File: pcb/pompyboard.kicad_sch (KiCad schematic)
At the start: 14 parts, among them J1 USB_C_Receptacle_USB2.0_16P, J2 Conn_01x04_Pin, SW1 EVQQ2B03W, U229 STM32F429IGT6, U231 AMS1117CD-3.3

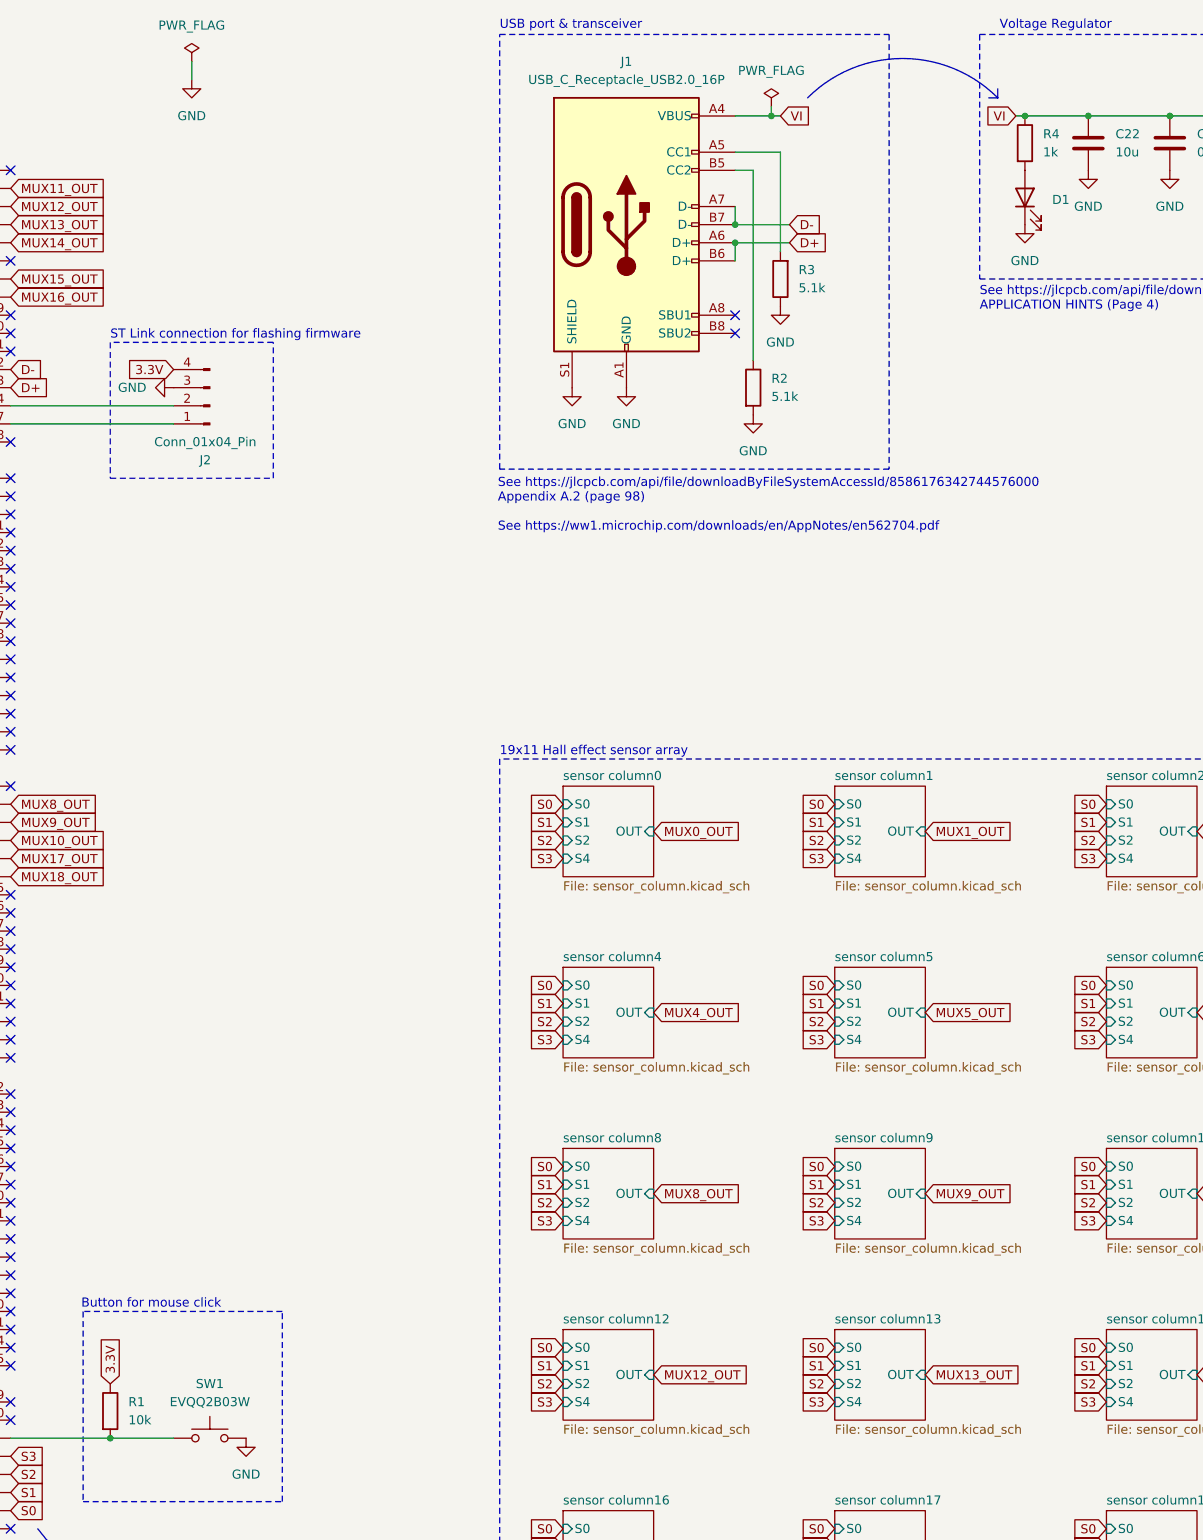
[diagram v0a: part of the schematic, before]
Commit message: pcb: add resistors to reduce multiplexer channel crosstalk
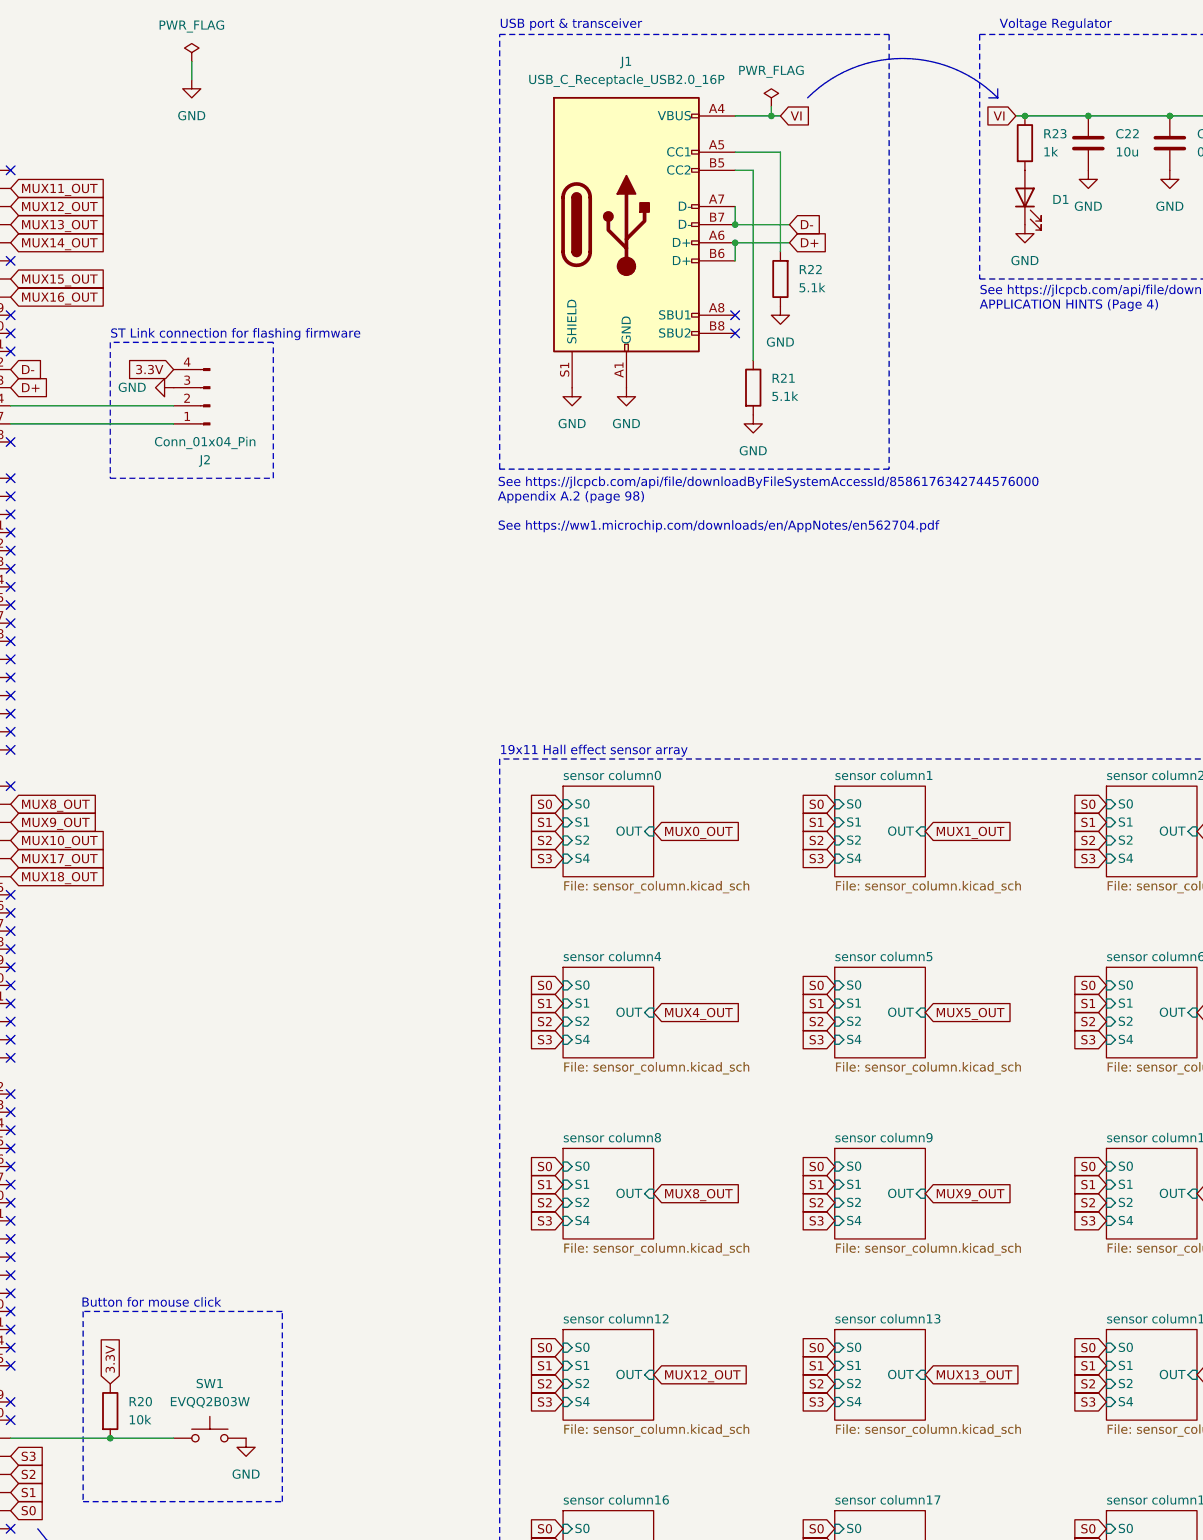
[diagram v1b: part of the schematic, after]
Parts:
- renumbered R1 to R20, R2 to R21, R3 to R22, R4 to R23
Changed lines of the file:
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@@
 		(dnp no)
 		(fields_autoplaced yes)
-		(property "Reference" "R3"
+		(property "Reference" "R22"
 			(at 219.71 58.4199 0)
 			(effects
@@
 			(project "pompyboard"
 				(path "/e5830f2e-b6bc-440e-bdf9-7651ab21e3a0"
-					(reference "R3")
+					(reference "R22")
 					(unit 1)
 				)
@@
 		(dnp no)
 		(fields_autoplaced yes)
-		(property "Reference" "R1"
+		(property "Reference" "R20"
 			(at 125.73 217.1699 0)
 			(effects
@@
 			(project ""
 				(path "/e5830f2e-b6bc-440e-bdf9-7651ab21e3a0"
-					(reference "R1")
+					(reference "R20")
 					(unit 1)
 				)
@@
 		(dnp no)
 		(fields_autoplaced yes)
-		(property "Reference" "R4"
+		(property "Reference" "R23"
 			(at 254 39.3699 0)
 			(effects
@@
 			(project "pompyboard"
 				(path "/e5830f2e-b6bc-440e-bdf9-7651ab21e3a0"
-					(reference "R4")
+					(reference "R23")
 					(unit 1)
 				)
@@
 		(dnp no)
 		(fields_autoplaced yes)
-		(property "Reference" "R2"
+		(property "Reference" "R21"
 			(at 215.9 73.6599 0)
 			(effects
@@
 			(project ""
 				(path "/e5830f2e-b6bc-440e-bdf9-7651ab21e3a0"
-					(reference "R2")
-					(unit 1)
-				)
+					(reference "R21")
+					(unit 1)
+				)

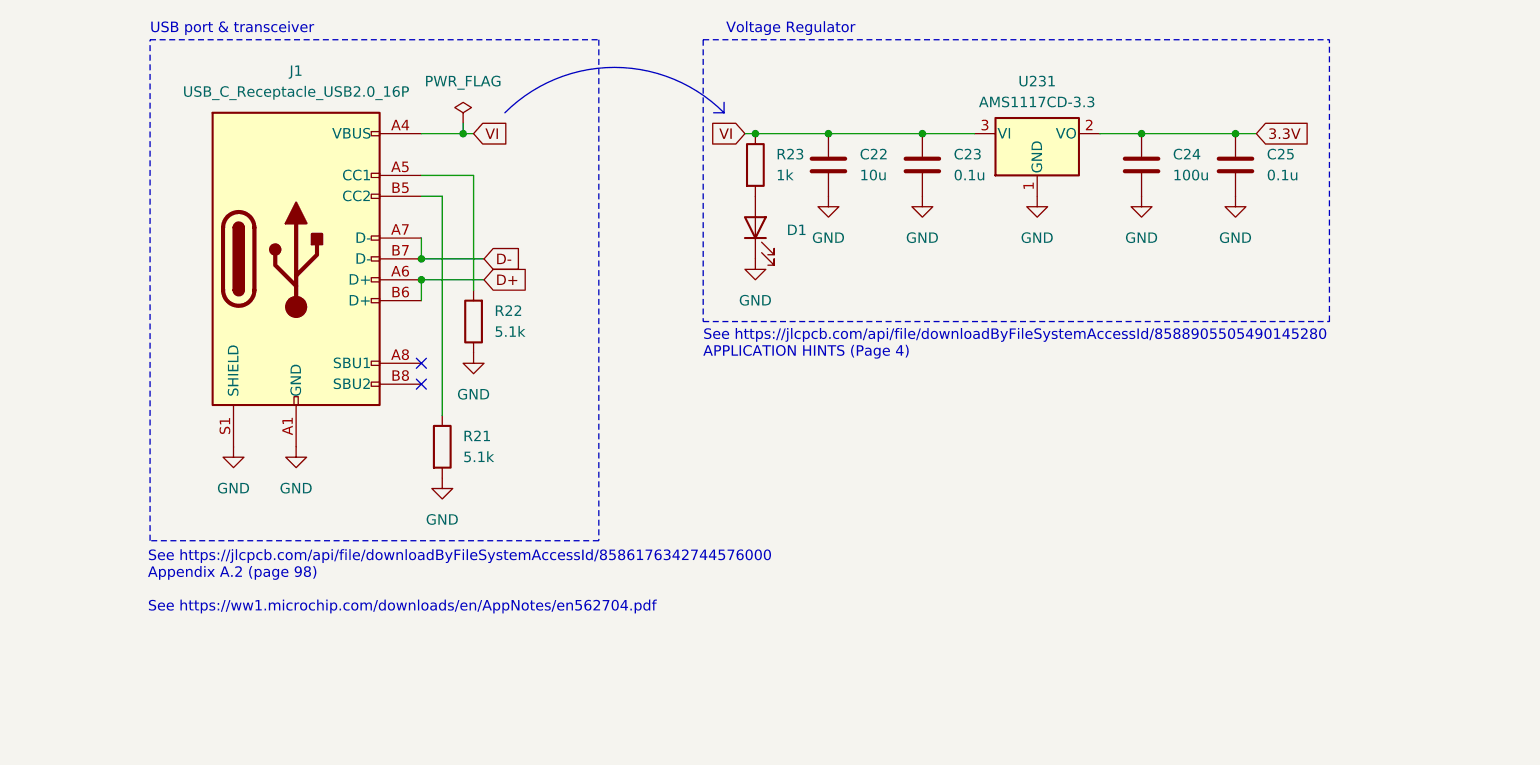
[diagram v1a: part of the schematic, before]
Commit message: pcb: replace LDO with buck converter to improve power efficiency
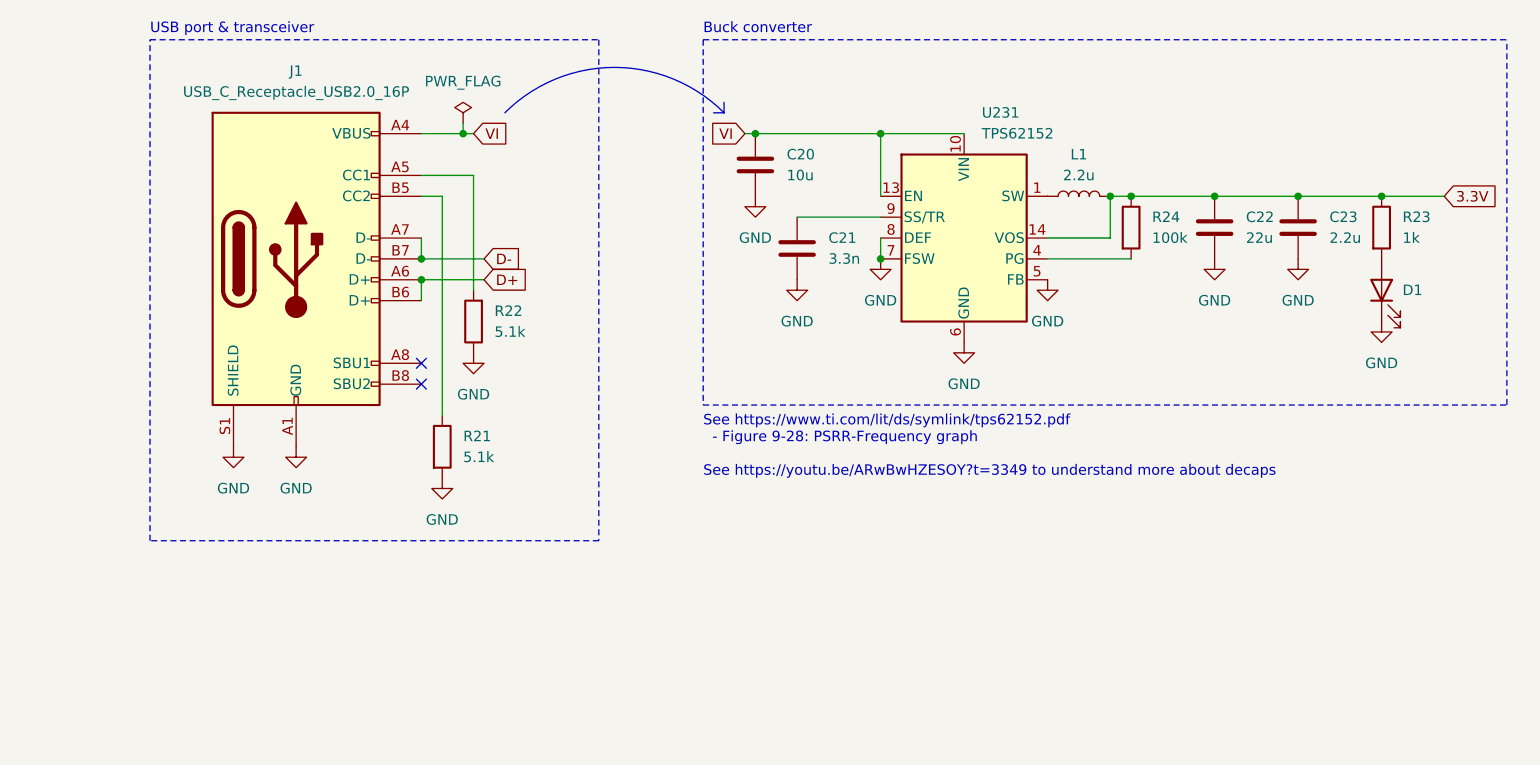
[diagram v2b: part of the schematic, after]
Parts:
- removed C25: 0.1u, Capacitor_SMD:C_0402_1005Metric, symbol Device:C
- removed U231: AMS1117CD-3.3, Package_TO_SOT_SMD:TO-252-3_TabPin2, symbol Regulator_Linear:AMS1117CD-3.3
- added C21: 3.3n, Capacitor_SMD:C_0402_1005Metric, symbol Device:C
- added L1: 2.2u, Inductor_SMD:L_Coilcraft_XxL4020, symbol Device:L
- added R24: 100k, Resistor_SMD:R_0603_1608Metric, symbol Device:R
- added U231: TPS62152, Package_DFN_QFN:VQFN-16-1EP_3x3mm_P0.5mm_EP1.68x1.68mm_ThermalVias, symbol Regulator_Switching:TPS62152
- C20: renamed from C22; footprint Capacitor_SMD:C_0603_1608Metric -> Capacitor_SMD:C_0402_1005Metric; LCSC Part # C19702 -> C315248
- C22: renamed from C24; value 100u -> 22u; footprint Capacitor_SMD:C_1206_3216Metric -> Capacitor_SMD:C_0402_1005Metric; LCSC Part # C6119960 -> C105226
- C23: value 0.1u -> 2.2u; footprint Capacitor_SMD:C_0402_1005Metric -> Capacitor_SMD:C_0201_0603Metric; LCSC Part # C1525 -> C335106
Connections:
- net 3.3V: now also C23.1, R23.1, L1.2, R24.1, U231.14 (VOS)
- net GND: now also C21.2, U231.15 (GND), U231.16 (GND), U231.17 (GND), U231.5 (FB), U231.6 (GND), U231.7 (FSW), U231.8 (DEF)
- net VI: now also U231.10 (VIN), U231.11 (VIN), U231.12 (VIN), U231.13 (EN); no longer C23.1, R23.1
- new net: C21.1, U231.9 (SS/TR)
- new net: L1.1, U231.1 (SW), U231.2 (SW), U231.3 (SW)
- new net: R24.2, U231.4 (PG)
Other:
- note added: "Buck converter"
- note added: "See https://www.ti.com/lit/ds/symlink/tps62152.pdf - Figure 9-28: PSRR-Frequency graph See https://youtu.be/ARwBwHZESOY?t=3349 to understand more about decaps"
- note removed: "See https://jlcpcb.com/api/file/downloadByFileSystemAccessId/8586176342744576000 Appendix A.2 (page 98) See https://ww1.microchip.com/downloads/en/AppNotes/en562704.pdf"
- note removed: "See https://jlcpcb.com/api/file/downloadByFileSystemAccessId/8588905505490145280 APPLICATION HINTS (Page 4)"
- note removed: "Voltage Regulator"
- moved on the sheet: C20, C22, D1, R23

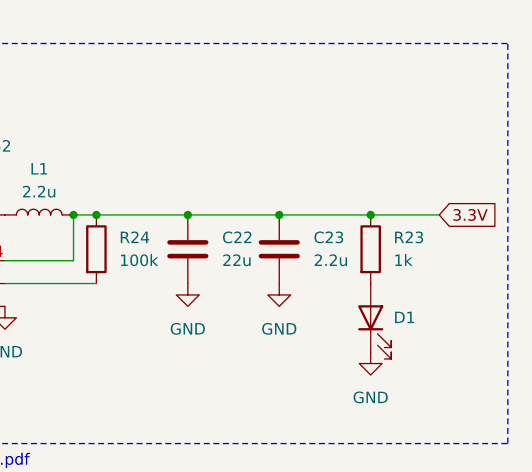
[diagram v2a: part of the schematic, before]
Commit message: pcb: add missing PWR_FLAG
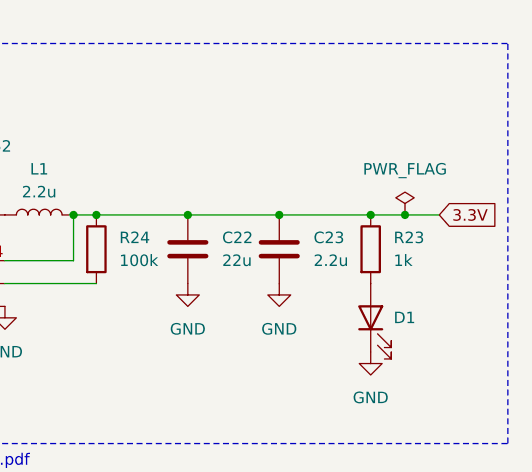
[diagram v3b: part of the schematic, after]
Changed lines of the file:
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@@
 	)
 	(junction
+		(at 331.47 44.45)
+		(diameter 0)
+		(color 0 0 0 0)
+	)
+	(junction
 		(at 215.9 36.83)
 		(diameter 0)
@@
 		)
 	)
+	(wire
+		(pts
+			(xy 331.47 44.45) (xy 335.28 44.45)
+		)
+		(stroke
+			(width 0)
+			(type default)
+		)
+	)
 	(polyline
 		(pts
@@
 	(wire
 		(pts
-			(xy 327.66 44.45) (xy 335.28 44.45)
+			(xy 327.66 44.45) (xy 331.47 44.45)
 		)
 		(stroke
@@
 					(unit 1)
 				)
+			)
+		)
+	)
+	(symbol
+		(lib_id "power:PWR_FLAG")
+		(at 331.47 44.45 0)
+		(unit 1)
+		(exclude_from_sim no)
+		(in_bom yes)
+		(on_board yes)
+		(dnp no)
+		(fields_autoplaced yes)
+		(property "Reference" "#FLG02"
+			(at 331.47 42.545 0)
+			(effects
+				(font
+					(size 1.27 1.27)
+				)
+				(hide yes)
+			)
+		)
+		(property "Value" "PWR_FLAG"
+			(at 331.47 39.37 0)
+			(effects
+				(font
+					(size 1.27 1.27)
+				)
+			)
+		)
+		(property "Footprint" ""
+			(at 331.47 44.45 0)
+			(effects
+				(font
+					(size 1.27 1.27)
+				)
+				(hide yes)
+			)
+		)
+		(property "Datasheet" "~"
+			(at 331.47 44.45 0)
+			(effects
+				(font
+					(size 1.27 1.27)
+				)
+				(hide yes)
+			)
+		)
+		(property "Description" "Special symbol for telling ERC where power comes from"
+			(at 331.47 44.45 0)
+			(effects
+				(font
+					(size 1.27 1.27)
+				)
+				(hide yes)
+			)
+		)
+		(pin "1"
+		)
+		(instances
+			(project "pompyboard"
+				(path "/e5830f2e-b6bc-440e-bdf9-7651ab21e3a0"
+					(reference "#FLG02")
+					(unit 1)
+				)
